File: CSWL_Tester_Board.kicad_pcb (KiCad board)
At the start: 2 copper layers, 204 parts, among them J1 Conn_02x10_Odd_Even, J2 Conn_01x03, J3 Conn_02x10_Odd_Even, J4 IDC 2.54mm, Q1 2N7002LT1G, Q2 2N7002LT1G, Q3 2N7002LT1G, Q4 2N7002LT1G, Q5 2N7002LT1G, Q6 2N7002LT1G, Q7 2N7002LT1G, Q8 2N7002LT1G, Q9 2N7002LT1G, U1 CD74HC4067M, U10 sn74hc595, U11 sn74hc595, U12 sn74hc595, U13 sn74hc595, U14 TCS3200, U15 TCS3200, U16 TCS3200, U17 TCS3200, U18 TCS3200, U19 TCS3200, U2 CD74HC4067M, U20 TCS3200, U21 TCS3200, U22 TCS3200, U23 TCS3200, U24 TCS3200, U25 TCS3200, U26 SN74HC151DR, U27 MCP1700T-3302E_TT, U28 SN74HC151DR, U29 74HC4016, U3 MCP1700T-3302E_TT, U4 sn74hc595, U5 sn74hc595, U6 sn74hc595, U7 STM32F103C8Tx, U8 sn74hc595, U9 sn74hc595, Y1 8MHz

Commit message: Ruan: start PCB design
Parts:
- added R125: 33R, Resistor_SMD:R_0603_1608Metric, F.Cu at (158.2, 29.6)
- added R126: 0R(NC), Resistor_SMD:R_0603_1608Metric, F.Cu at (192.4, 36.5)
- added R127: 0R(NC), Resistor_SMD:R_0603_1608Metric, F.Cu at (202.4, 36.3)
- added R128: 0R(NC), Resistor_SMD:R_0603_1608Metric, F.Cu at (178.2, 36.5)
- added R129: 0R(NC), Resistor_SMD:R_0603_1608Metric, F.Cu at (209.5, 36.4)
- added R130: 0R(NC), Resistor_SMD:R_0603_1608Metric, F.Cu at (185.2, 36.4)
- C11, C12: value 20pF -> 22pF
- R13, R14, R15, R16, R17, R18, R25, R26, R27, R28, R29, R30: value 10K -> 680R
- U14, U15, U16, U17, U18, U19, U20, U21, U22, U23, U24, U25: moved to B.Cu
- Y1: value 8MHz -> Crystal_GND24; footprint Crystal:Crystal_SMD_3225-4Pin_3.2x2.5mm_HandSoldering -> RuanProject:Crystal_SMD_3225-4Pin_3.2x2.5mm_HandSoldering
- moved U2 198.4 mm to (203.5, 24.2), turned to 90 degrees
- moved U12 192.5 mm to (204.6, 109.7)
- moved D12 187.0 mm to (196.8, 74.8)
- moved D10 186.3 mm to (198.6, 119.0)
- moved J1 179.6 mm to (183.1, 13.5), turned to 90 degrees
- moved D3 178.7 mm to (179.7, 136.1)
- moved U6 173.7 mm to (176.8, 142.7), turned to 270 degrees
- moved Q1 172.4 mm to (212.4, 36.7), turned to 90 degrees
- moved U13 170.2 mm to (204.7, 84.9)
- moved R12 167.2 mm to (207.7, 32.1), turned to 270 degrees
- moved U5 167.0 mm to (142.1, 143.7), turned to 270 degrees
- moved D11 166.1 mm to (206.5, 95.7)
- moved D2 165.0 mm to (157.9, 140.4)
- moved R29 164.8 mm to (206.6, 98.9)
- moved U20 162.9 mm to (189.5, 114.2), turned to 90 degrees
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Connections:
- C23 pad 1: Net-(C23-Pad1) -> GND
- C24 pad 1: Net-(C23-Pad1) -> GND
- C3 pad 1: Net-(C3-Pad1) -> GND
- C5 pad 1: Net-(C3-Pad1) -> GND
- J1 pad 7: /LED4+ -> /LED11+
- J1 pad 8: /LED4- -> /LED11-
- J3 pad 1: /LED11+ -> /LED4+
- J3 pad 10: /CSWL_Vout- -> /CSWL_IN+
- J3 pad 11: /CSWL_Vout+ -> /CSWL_VDD-
- J3 pad 12: /CSWL_Vout- -> /CSWL_IN+
- J3 pad 13: /CSWL_IN+ -> /TP300
- J3 pad 15: /CSWL_IN+ -> /TP303
- J3 pad 2: /LED11- -> /CSWL_Vout-
- J3 pad 3: /LED12+ -> /LED4-
- J3 pad 4: /LED12- -> /CSWL_Vout-
- J3 pad 5: /TP300 -> /LED12+
- J3 pad 6: /TP303 -> /CSWL_Vout+
- J3 pad 7: /CSWL_VDD+ -> /LED12-
- J3 pad 8: /CSWL_VDD- -> /CSWL_Vout+
- J3 pad 9: /CSWL_Vout+ -> /CSWL_VDD+
- J4 pad 1: /CSWL_Vout+ -> /CSWL_Vout-
- J4 pad 10: /GB14 -> GND
- J4 pad 11: /CSWL_IN- -> /CSWL_IN+
- J4 pad 12: /GB13 -> GND
- J4 pad 13: /CSWL_IN+ -> /CSWL_IN-
- J4 pad 15: /CSWL_IN+ -> /CSWL_IN-
- J4 pad 17: /VMeter+ -> /VMeter-
- J4 pad 19: /VMeter- -> /VMeter+
- J4 pad 3: /CSWL_Vout+ -> /CSWL_Vout-
- J4 pad 4: /LED_UsartTx -> +5V
- J4 pad 5: /CSWL_Vout- -> /CSWL_Vout+
- J4 pad 6: /LED_UsartRx -> /LED_UsartTx
- J4 pad 7: /CSWL_Vout- -> /CSWL_Vout+
- J4 pad 8: GND -> /LED_UsartRx
- J4 pad 9: /CSWL_IN- -> /CSWL_IN+
- R112 pad 1: GND -> GNDA
- R112 pad 2: Net-(R112-Pad2) -> GND
- R117 pad 1: GND -> GNDA
- R13 pad 1: VCC33_B -> VCC33_A
- R14 pad 1: VCC33_B -> VCC33_A
- R15 pad 1: VCC33_B -> VCC33_A
- R16 pad 1: VCC33_B -> VCC33_A
- R17 pad 1: VCC33_B -> VCC33_A
- R18 pad 1: VCC33_B -> VCC33_A
- R25 pad 1: VCC33_B -> VCC33_A
- R26 pad 1: VCC33_B -> VCC33_A
- R27 pad 1: VCC33_B -> VCC33_A
- R28 pad 1: VCC33_B -> VCC33_A
- R29 pad 1: VCC33_B -> VCC33_A
- R30 pad 1: VCC33_B -> VCC33_A
- R49 pad 1: GND -> GNDA
- R51 pad 1: GND -> GNDA
- R53 pad 1: GND -> GNDA
- R55 pad 1: GND -> GNDA
- R57 pad 1: GND -> GNDA
- R79 pad 1: GND -> GNDA
- R81 pad 1: GND -> GNDA
- R83 pad 1: GND -> GNDA
- R85 pad 1: GND -> GNDA
- R87 pad 1: GND -> GNDA
- R89 pad 1: GND -> GNDA
- U29 pad 1: /CSWL_VDD+ -> Net-(R125-Pad1)
- U29 pad 12: /CSWL_TestMode_SN -> /TestMode_SN
- U29 pad 13: /CSWL_TestMode_S2 -> /TestMode_S2
- U29 pad 4: /CSWL_VDD+ -> Net-(R125-Pad1)
- U29 pad 5: /CSWL_TestMode_S3 -> /TestMode_S3
- U29 pad 6: /CSWL_TestMode_S4 -> /TestMode_S4
- U29 pad 8: /CSWL_VDD+ -> Net-(R125-Pad1)
- Y1 pad 2: Net-(C12-Pad2) -> GND
- Y1 pad 3: (no net) -> Net-(C12-Pad2)
- Y1 pad 4: (no net) -> GND
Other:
- board text added: "TP107"
- board text added: "TP108"
- board text added: "TP109"
- board text added: "TP110"
- board text added: "TP111"
- board text added: "TP200"
- board text added: "TP201"
- board text added: "TP300"
- board text added: "TP303"
- board text added: "TP306"
- board text added: "TP310"
- board text added: "TP311"

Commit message: Ruan: pcb designing
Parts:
- R111, R112, R113, R114, R115, R116, R119, R120, R121, R122, R123, R124: moved to B.Cu
- moved C14 39.4 mm to (90.5, 49.2), turned to 270 degrees
- moved C23 32.0 mm to (92.9, 31.0)
- moved C24 32.0 mm to (95.7, 33.9)
- moved U27 32.0 mm to (95.7, 31.1)
- moved C13 31.8 mm to (92.4, 40.3), turned to 270 degrees
- moved C16 30.6 mm to (100.7, 54.0), turned to 0 degrees
- moved U3 28.1 mm to (94.4, 23.8)
- moved C3 28.1 mm to (91.5, 23.6)
- moved C5 28.1 mm to (94.3, 26.8)
- moved R5 28.1 mm to (98.0, 24.9)
- moved C15 27.9 mm to (100.6, 52.3), turned to 0 degrees
- moved U7 24.5 mm to (97.2, 45.9), turned to 180 degrees
- moved R17 21.1 mm to (125.1, 113.5), turned to 0 degrees
- moved R62 19.1 mm to (201.9, 128.3), turned to 270 degrees
- moved R115 18.9 mm to (174.1, 50.7), turned to 270 degrees
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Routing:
- net GNDA: track 0.00 -> 226.8 mm, vias 0 -> 18
- net VCC33_B: track 0.00 -> 183.5 mm, vias 0 -> 13
- net VCC33_A: track 0.00 -> 144.4 mm, vias 0 -> 6
- net /LED5_S0: track 0.00 -> 42.9 mm, vias 0 -> 3
- net /LED10_S3: track 0.00 -> 40.8 mm, vias 0 -> 3
- net /LED8_S2: track 0.00 -> 39.7 mm, vias 0 -> 2
- net /LED1_S3: track 0.00 -> 39.1 mm, vias 0 -> 1
- net /LED11_EN: track 0.00 -> 38.9 mm, vias 0 -> 1
- net /LED9_EN: track 0.00 -> 38.7 mm, vias 0 -> 3
- net /LED9_S0: track 0.00 -> 36.3 mm, vias 0 -> 3
- net /LED8_S3: track 0.00 -> 34.9 mm, vias 0 -> 1
- net /LED3_OUT: track 0.00 -> 34.8 mm
- net /LED10_S1: track 0.00 -> 33.7 mm, vias 0 -> 2
- net /LED6_EN: track 0.00 -> 33.6 mm, vias 0 -> 1
- net /LED10_S2: track 0.00 -> 33.5 mm, vias 0 -> 1
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
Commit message: Ruan： PCB designing
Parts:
- moved C23 32.0 mm to (121.0, 15.6)
- moved C24 32.0 mm to (123.8, 18.6)
- moved U27 32.0 mm to (123.8, 15.8)
- moved C3 21.5 mm to (111.5, 15.5)
- moved C5 21.5 mm to (114.3, 18.7)
- moved U3 21.5 mm to (114.4, 15.7)
- moved R5 21.3 mm to (118.9, 20.8)
- moved Y1 13.5 mm to (117.6, 37.8)
- moved C11 13.5 mm to (116.9, 41.0)
- moved C14 13.5 mm to (101.8, 41.9)
- moved C16 13.5 mm to (112.0, 46.6)
- moved R10 13.5 mm to (114.7, 45.9)
- moved C13 13.5 mm to (103.7, 33.0)
- moved C15 13.5 mm to (111.9, 45.0)
- moved U7 13.5 mm to (108.5, 38.6)
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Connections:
- U7 pad 40: /Serial_CLK -> /Serial_Input
- U7 pad 41: /Serial_Input -> /Serial_nEN
- U7 pad 42: /Serial_nEN -> /Shift_reg_lock
- U7 pad 43: /Shift_reg_lock -> /Serial_CLK
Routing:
- net /Serial_nEN: track 0.00 -> 476.9 mm, vias 0 -> 16
- net /Shift_reg_lock: track 0.00 -> 459.0 mm, vias 0 -> 16
- net /Serial_CLK: track 0.00 -> 443.6 mm, vias 0 -> 16
- net /Shift_reg_clear: track 0.00 -> 427.6 mm, vias 0 -> 6
- net /Serial_Ouput: track 0.00 -> 232.6 mm, vias 0 -> 2
- net /Serial_Input: track 0.00 -> 187.7 mm, vias 0 -> 2
- net VCC33_A: track 144.4 -> 259.8 mm, vias 6 -> 8
- net /LED_7-12_S2: track 0.00 -> 114.0 mm, vias 0 -> 2
- net /LED_7-12_S1: track 0.00 -> 111.1 mm, vias 0 -> 2
- net /LED_7-12_S0: track 0.00 -> 108.5 mm, vias 0 -> 2
- net /LED_1-6_S2: track 0.00 -> 103.0 mm, vias 0 -> 4
- net /LED_1-6_S1: track 0.00 -> 101.0 mm, vias 0 -> 4
- net /LED_1-6_S0: track 0.00 -> 100.9 mm, vias 0 -> 4
- net /LED1_OUT: track 19.9 -> 116.2 mm, vias 0 -> 1
- net /LED12_OUT: track 16.6 -> 107.6 mm, vias 0 -> 3
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
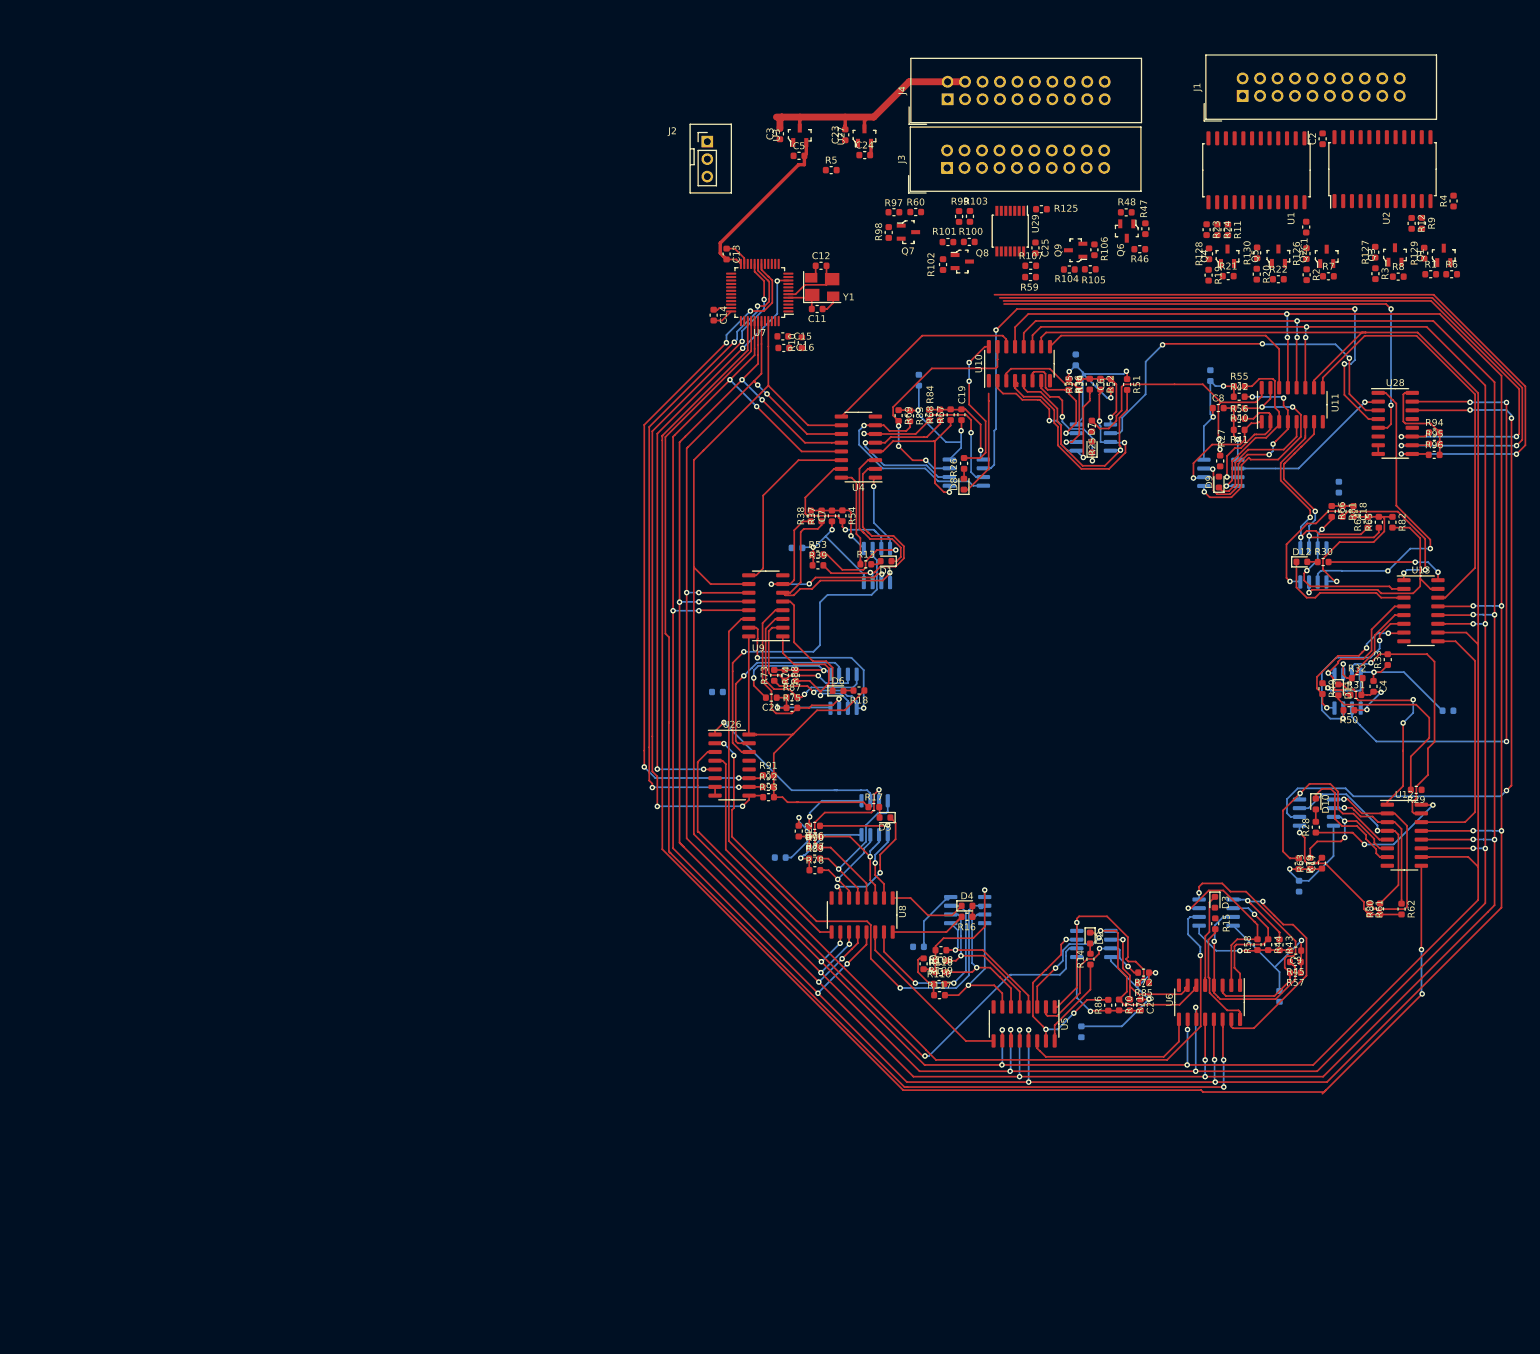
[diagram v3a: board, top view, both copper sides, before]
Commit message: Ruan: PCB design -> base layout finish
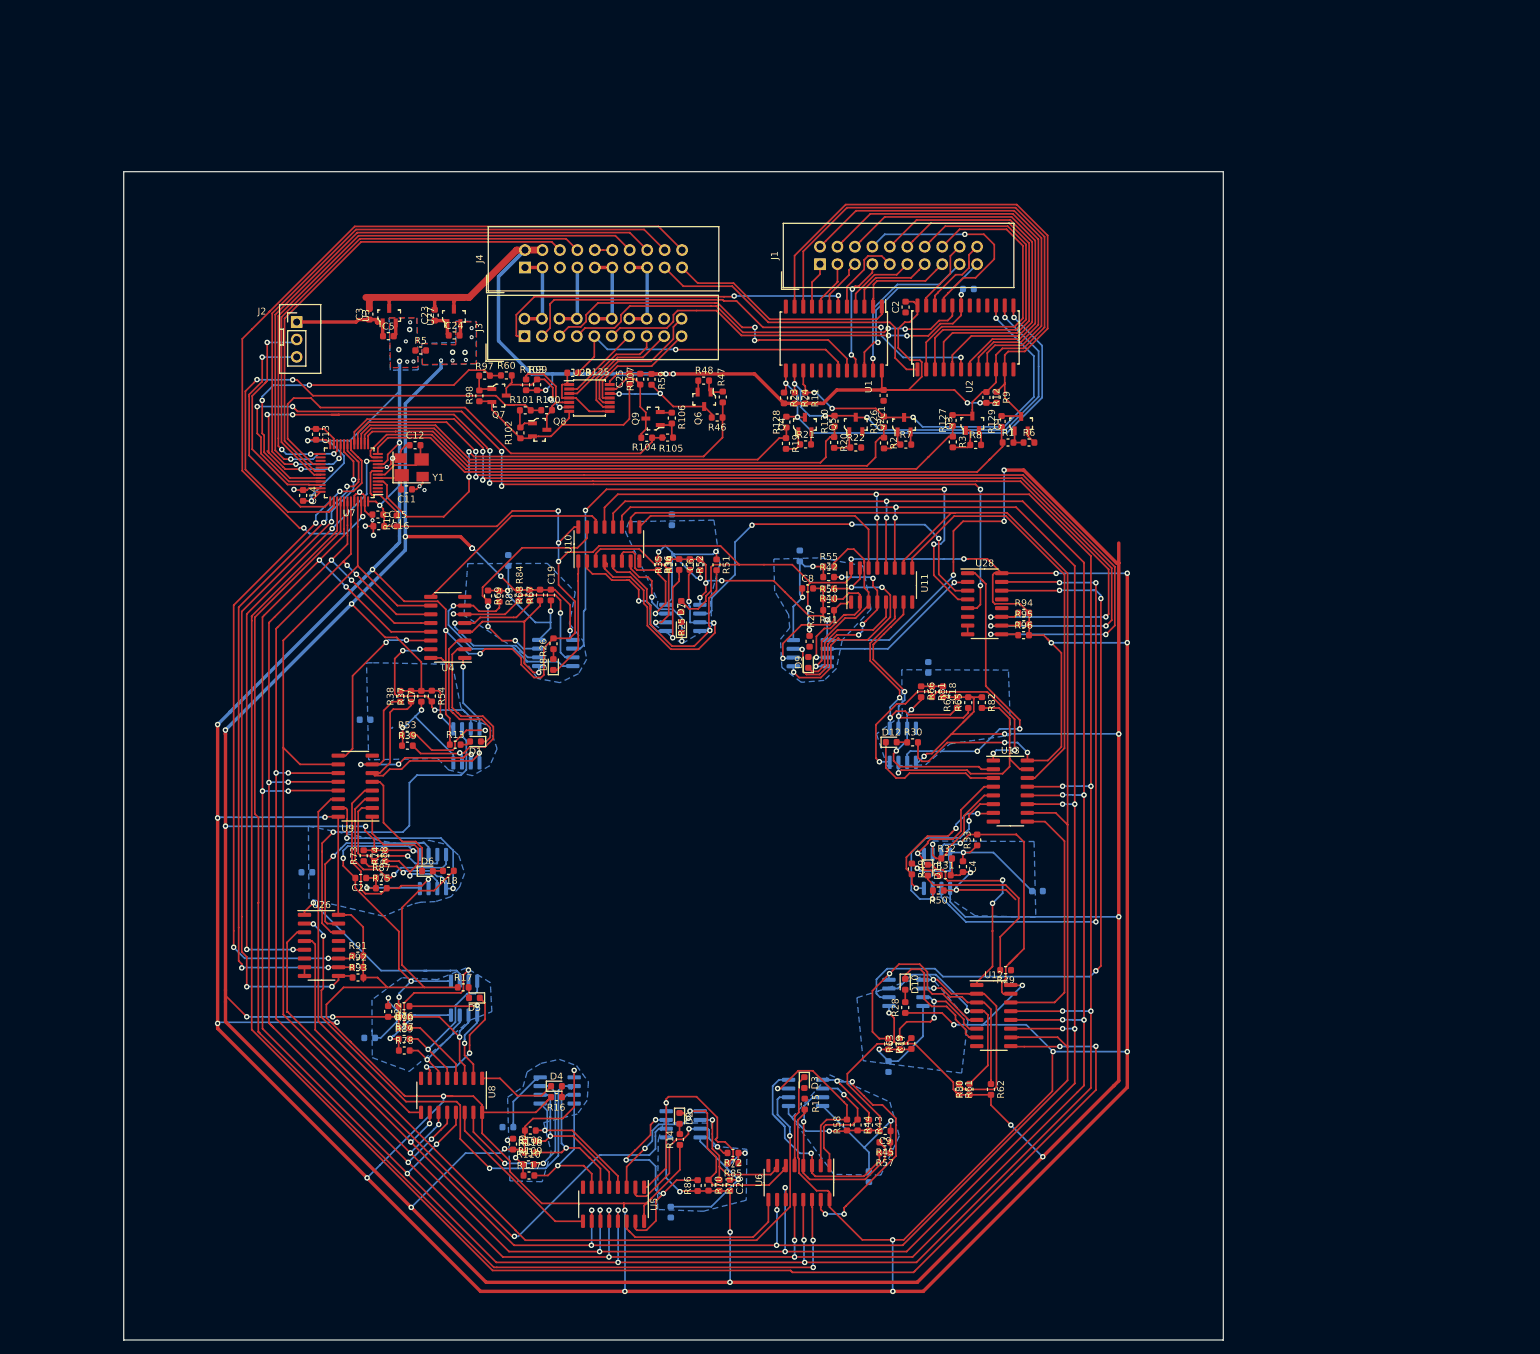
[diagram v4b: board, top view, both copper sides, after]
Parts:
- R4: moved to B.Cu
- moved R125 72.2 mm to (81.3, 50.3)
- moved R4 71.7 mm to (138.9, 38.1), turned to 180 degrees
- moved R103 69.1 mm to (74.5, 52.0)
- moved R114 67.6 mm to (51.1, 100.7)
- moved R9 66.9 mm to (143.0, 53.8)
- moved R12 66.9 mm to (141.5, 53.8)
- moved J3 66.2 mm to (74.3, 44.9)
- moved J4 66.2 mm to (74.4, 34.9)
- moved Q1 66.2 mm to (146.6, 57.7)
- moved Q2 66.2 mm to (129.5, 57.8)
- moved Q3 66.2 mm to (139.5, 57.6)
- moved Q4 66.2 mm to (115.1, 57.8)
- moved Q5 66.2 mm to (122.5, 57.8)
- moved Q6 66.2 mm to (100.5, 54.1)
- moved Q8 66.2 mm to (76.5, 58.6)
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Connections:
- U7 pad 13: /Switchs_S2 -> /Switchs_EN
- U7 pad 14: /Switchs_S3 -> /Switchs_S2
- U7 pad 15: /Switchs_EN -> /Switchs_S3
- U7 pad 16: /LED_7-12_S0 -> /LED_7-12_S2
- U7 pad 29: /LED_7-12_S2 -> /LED_7-12_S0
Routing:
- net VCC33_A: track 259.8 -> 1040.7 mm, vias 8 -> 42
- net VCC33_B: track 200.8 -> 858.9 mm, vias 14 -> 46
- net +5V: track 37.5 -> 184.1 mm, vias 0 -> 6
- net /GB9: track 0.00 -> 116.2 mm, vias 0 -> 2
- net /Switchs_S1: track 0.00 -> 99.2 mm
- net /GB10: track 0.00 -> 96.5 mm, vias 0 -> 2
- net /Switchs_S0: track 0.00 -> 93.2 mm
- net /GB11: track 0.00 -> 90.8 mm, vias 0 -> 2
- net GND: track 14.1 -> 99.6 mm, vias 0 -> 10
- net /S1: track 0.00 -> 85.2 mm
- net /Switchs_EN: track 0.00 -> 83.1 mm
- net /S0: track 0.00 -> 83.0 mm
- net /GB12: track 0.00 -> 82.4 mm, vias 0 -> 2
- net /Switchs_S2: track 0.00 -> 76.6 mm
- net /CSWL_TestMode_S3: track 0.00 -> 74.4 mm, vias 0 -> 2
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- added copper zone on B.Cu, net GNDA
- added copper zone on B.Cu, net VCC33_A
- added copper zone on F.Cu, net VCC33_A
- added copper zone on B.Cu, net VCC33_B
- added copper zone on F.Cu, net VCC33_B
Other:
- board outline added: 160 x 170 mm

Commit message: Ruan: base ok
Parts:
- added TP1: Location Point, RuanProject:Local_Hole_D5.0mm_Drill3.5mm, F.Cu at (36.0, 171.0)
- added TP2: Location Point, RuanProject:Local_Hole_D5.0mm_Drill3.5mm, F.Cu at (156.0, 171.0)
- added TP3: Location Point, RuanProject:Local_Hole_D5.0mm_Drill3.5mm, F.Cu at (166.0, 31.0)
- added TP4: Location Point, RuanProject:Local_Hole_D5.0mm_Drill3.5mm, F.Cu at (26.0, 31.0)
- moved D1 0.08 mm to (67.3, 103.9)
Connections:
- C10 pad 1: GNDA -> GNDA3
- C17 pad 1: GNDA -> GNDA12
- C18 pad 1: GNDA -> GNDA10
- C19 pad 1: GNDA -> GNDA7
- C20 pad 1: GNDA -> GNDA2
- C21 pad 1: GNDA -> GNDA5
- C22 pad 1: GNDA -> GNDA4
- C4 pad 1: GNDA -> GNDA11
- C6 pad 1: GNDA -> GNDA8
- C7 pad 1: GNDA -> GNDA6
- C8 pad 1: GNDA -> GNDA9
- C9 pad 1: GNDA -> GNDA1
- R110 pad 1: GNDA -> GNDA3
- R111 pad 2: GNDA -> GNDA3
- R112 pad 1: GNDA -> GNDA8
- R113 pad 2: GNDA -> GNDA11
- R114 pad 2: GNDA -> GNDA6
- R115 pad 2: GNDA -> GNDA9
- R116 pad 2: GNDA -> GNDA1
- R117 pad 1: GNDA -> GNDA3
- R119 pad 2: GNDA -> GNDA12
- R120 pad 2: GNDA -> GNDA10
- R121 pad 2: GNDA -> GNDA2
- R122 pad 1: GNDA -> GNDA5
- R123 pad 2: GNDA -> GNDA7
- R124 pad 2: GNDA -> GNDA4
- R33 pad 1: GNDA -> GNDA11
- R36 pad 1: GNDA -> GNDA8
- R39 pad 1: GNDA -> GNDA6
- R42 pad 1: GNDA -> GNDA9
- R45 pad 1: GNDA -> GNDA1
- R49 pad 1: GNDA -> GNDA11
- R51 pad 1: GNDA -> GNDA8
- R53 pad 1: GNDA -> GNDA6
- R55 pad 1: GNDA -> GNDA9
- R57 pad 1: GNDA -> GNDA1
- R63 pad 1: GNDA -> GNDA12
- R66 pad 1: GNDA -> GNDA10
- R69 pad 1: GNDA -> GNDA7
- R72 pad 1: GNDA -> GNDA2
- R75 pad 1: GNDA -> GNDA5
- R78 pad 1: GNDA -> GNDA4
- R79 pad 1: GNDA -> GNDA12
- R81 pad 1: GNDA -> GNDA10
- R83 pad 1: GNDA -> GNDA7
- R85 pad 1: GNDA -> GNDA2
- R87 pad 1: GNDA -> GNDA5
- R89 pad 1: GNDA -> GNDA4
- U14 pad 4: GNDA -> GNDA11
- U15 pad 4: GNDA -> GNDA8
- U16 pad 4: GNDA -> GNDA6
- U17 pad 4: GNDA -> GNDA9
- U18 pad 4: GNDA -> GNDA1
- U19 pad 4: GNDA -> GNDA3
- U20 pad 4: GNDA -> GNDA12
- U21 pad 4: GNDA -> GNDA10
- U22 pad 4: GNDA -> GNDA7
- U23 pad 4: GNDA -> GNDA2
- U24 pad 4: GNDA -> GNDA5
- U25 pad 4: GNDA -> GNDA4
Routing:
- net GND: track 99.6 -> 1417.6 mm, vias 10 -> 128
- net GNDA: track 232.7 -> 0.00 mm, vias 20 -> 0
- net VCC33_A: track 1040.7 -> 1077.2 mm
- net GNDA8: track 0.00 -> 36.3 mm, vias 0 -> 3
- net GNDA2: track 0.00 -> 28.0 mm, vias 0 -> 2
- net GNDA11: track 0.00 -> 27.5 mm, vias 0 -> 2
- net GNDA6: track 0.00 -> 27.5 mm, vias 0 -> 2
- net GNDA4: track 0.00 -> 27.4 mm, vias 0 -> 2
- net GNDA1: track 0.00 -> 25.7 mm, vias 0 -> 1
- net GNDA7: track 0.00 -> 24.3 mm, vias 0 -> 2
- net GNDA5: track 0.00 -> 23.7 mm, vias 0 -> 1
- net GNDA9: track 0.00 -> 22.4 mm, vias 0 -> 2
- net GNDA12: track 0.00 -> 20.6 mm, vias 0 -> 1
- net GNDA3: track 0.00 -> 19.9 mm, vias 0 -> 2
- net GNDA10: track 0.00 -> 12.8 mm, vias 0 -> 1
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- added copper zone on B.Cu, net GND
- added copper zone on F.Cu, net GND
- added copper zone on B.Cu, net GNDA1
- added copper zone on B.Cu, net GNDA10
- added copper zone on B.Cu, net GNDA11
- added copper zone on B.Cu, net GNDA12
- added copper zone on B.Cu, net GNDA2
- added copper zone on B.Cu, net GNDA3
- added copper zone on B.Cu, net GNDA4
- added copper zone on B.Cu, net GNDA5
- added copper zone on B.Cu, net GNDA6
- added copper zone on B.Cu, net GNDA7
- added copper zone on B.Cu, net GNDA8
- added copper zone on B.Cu, net GNDA9
- removed copper zone on B.Cu, net GNDA
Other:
- outline, holes or cut-outs redrawn
- board text added: "TP331"
- board text added: "TP332"

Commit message: Ruan: base ok
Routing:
- net /LED8_S2: track 41.3 -> 25.3 mm, vias 2 -> 1
- net VCC33_B: track 862.2 -> 853.0 mm
- net /LED6_OUT: track 49.9 -> 58.7 mm
- net VCC33_A: track 1077.2 -> 1070.9 mm
- net /LED7_S0: track 23.0 -> 27.5 mm
- net /LED11_S3: track 21.9 -> 24.7 mm, vias 3 -> 2
- net /LED10_S0: track 33.0 -> 35.5 mm
- net /LED2_S3: track 33.3 -> 31.3 mm
- net /LED8_S0: track 30.5 -> 32.2 mm
- net /LED1_S3: track 32.7 -> 31.3 mm
- net /LED10_EN: track 26.0 -> 24.5 mm
- net /LED11_S2: track 28.0 -> 29.4 mm
- net /LED11_S1: track 17.5 -> 18.8 mm
- net /LED2_S0: track 27.8 -> 26.7 mm
- net /LED10_S3: track 40.8 -> 39.9 mm
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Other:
- outline, holes or cut-outs redrawn
- board text removed: "TP107"
- board text removed: "TP108"
- board text removed: "TP109"
- board text removed: "TP110"
- board text removed: "TP111"
- board text removed: "TP200"
- board text removed: "TP201"
- board text removed: "TP300"
- board text removed: "TP303"
- board text removed: "TP306"
- board text removed: "TP310"
- board text removed: "TP311"
- board text removed: "TP331"
- board text removed: "TP332"

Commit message: Ruan: modify shape
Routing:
- net /LED4_S2: track 29.2 -> 26.5 mm
